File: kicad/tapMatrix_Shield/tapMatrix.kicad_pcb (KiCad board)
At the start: 2 copper layers, 68.6 x 53.3 mm, 28 parts, among them IC1 DS1307, P5 TS_ZIF, P6 LED_MATRIX_HDR, P7 SPKR, U1 APE8865N-33-HF-3, U2 MCP4921-E/SN, U3 74LS125, U4 TL072, U5 SD_CARD

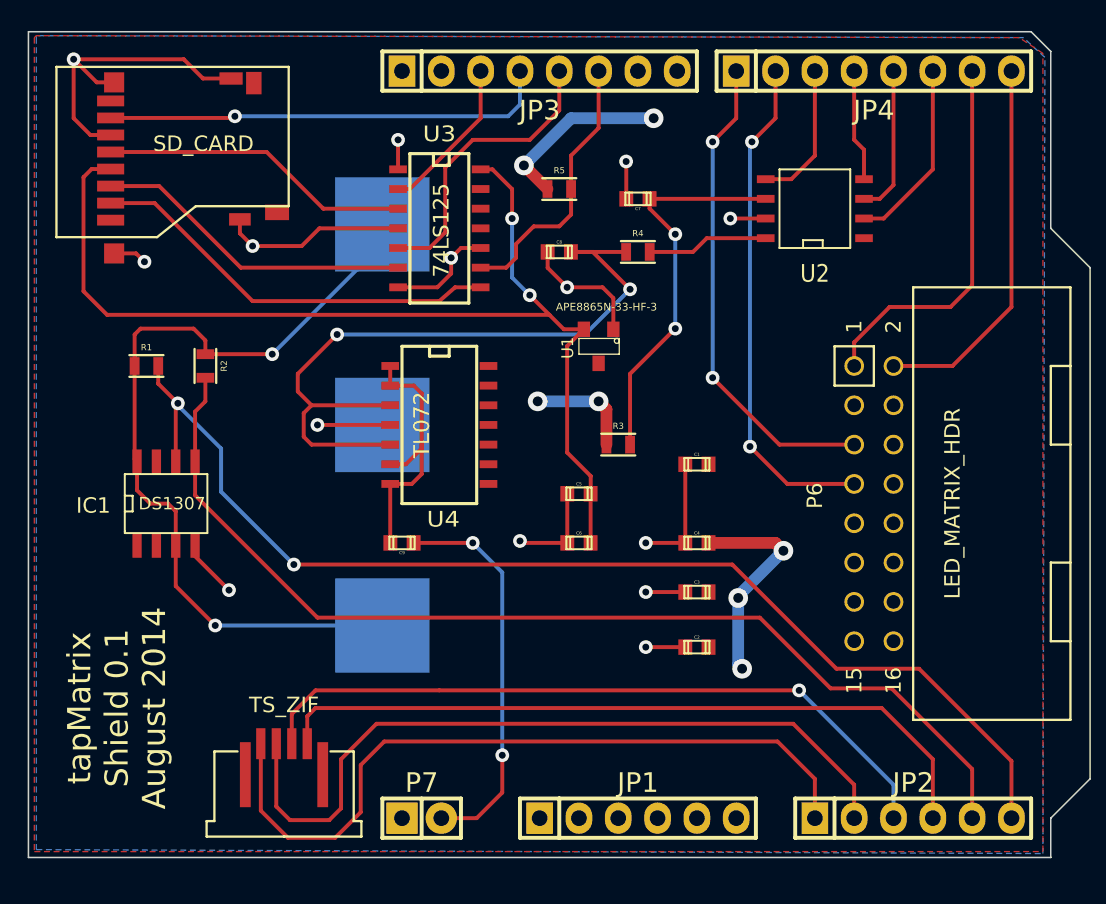
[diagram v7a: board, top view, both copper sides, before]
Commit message: replaced 100uF caps with avail footprint; moved vias; revised to 0.2;
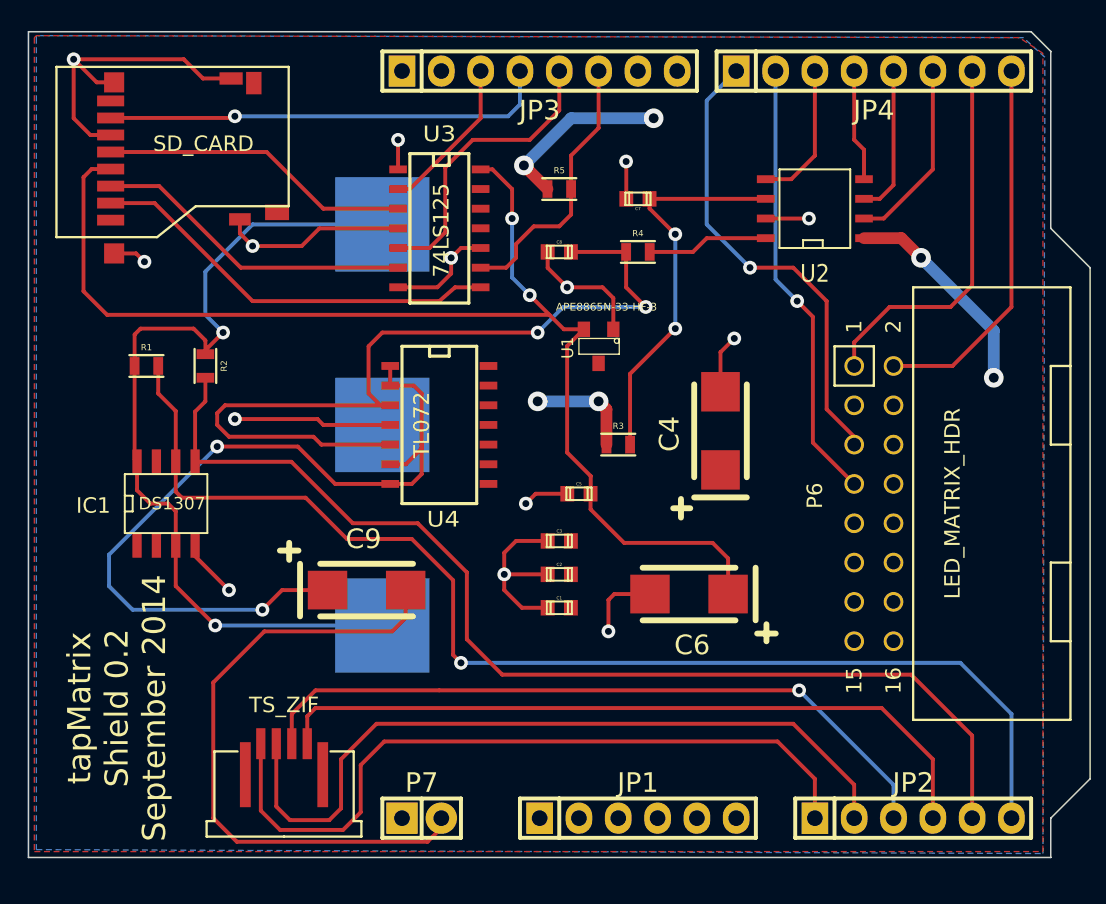
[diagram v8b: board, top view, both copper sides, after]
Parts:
- C4, C6, C9: footprint Capacitors_SMD:c_0603 -> Capacitors_Tantalum_SMD:TantalC_SizeC_EIA-6032_Reflow
- moved C1 12.8 mm to (165.1, 123.6)
- moved C2 10.1 mm to (165.1, 121.4)
- moved C3 9.48 mm to (165.1, 119.3)
- moved C6 7.84 mm to (173.5, 122.7), turned to 180 degrees
- moved C4 7.40 mm to (175.5, 112.1), turned to 90 degrees
- moved C9 3.81 mm to (152.7, 122.4), turned to 0 degrees
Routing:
- net Net-(C9-Pad1): track 17.5 -> 53.1 mm, vias 0 -> 2
- net Net-(C9-Pad2): track 25.4 -> 41.1 mm, vias 2 -> 0
- net +3.3V: track 69.2 -> 79.6 mm
- net GND: track 83.9 -> 94.1 mm
- net Net-(C8-Pad1): track 47.6 -> 55.2 mm
- net Net-(BT1-Pad1): track 54.0 -> 58.6 mm
- net /MATRIX_DATA: track 32.7 -> 28.8 mm, vias 2 -> 1
- net /I2C_SDA: track 68.6 -> 71.1 mm
- net /I2C_SCL: track 75.6 -> 78.1 mm, vias 2 -> 1
- net /MATRIX_WR: track 31.4 -> 30.5 mm, vias 2 -> 1
- net +5V: track 32.7 -> 32.6 mm, vias 7 -> 6
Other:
- board text added: "tapMatrix Shield 0.2 September 2014"
- board text removed: "tapMatrix Shield 0.1 August 2014"
